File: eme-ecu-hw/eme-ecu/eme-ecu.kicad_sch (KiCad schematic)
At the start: 11 parts, among them U1 ACS712xLCTR-30A

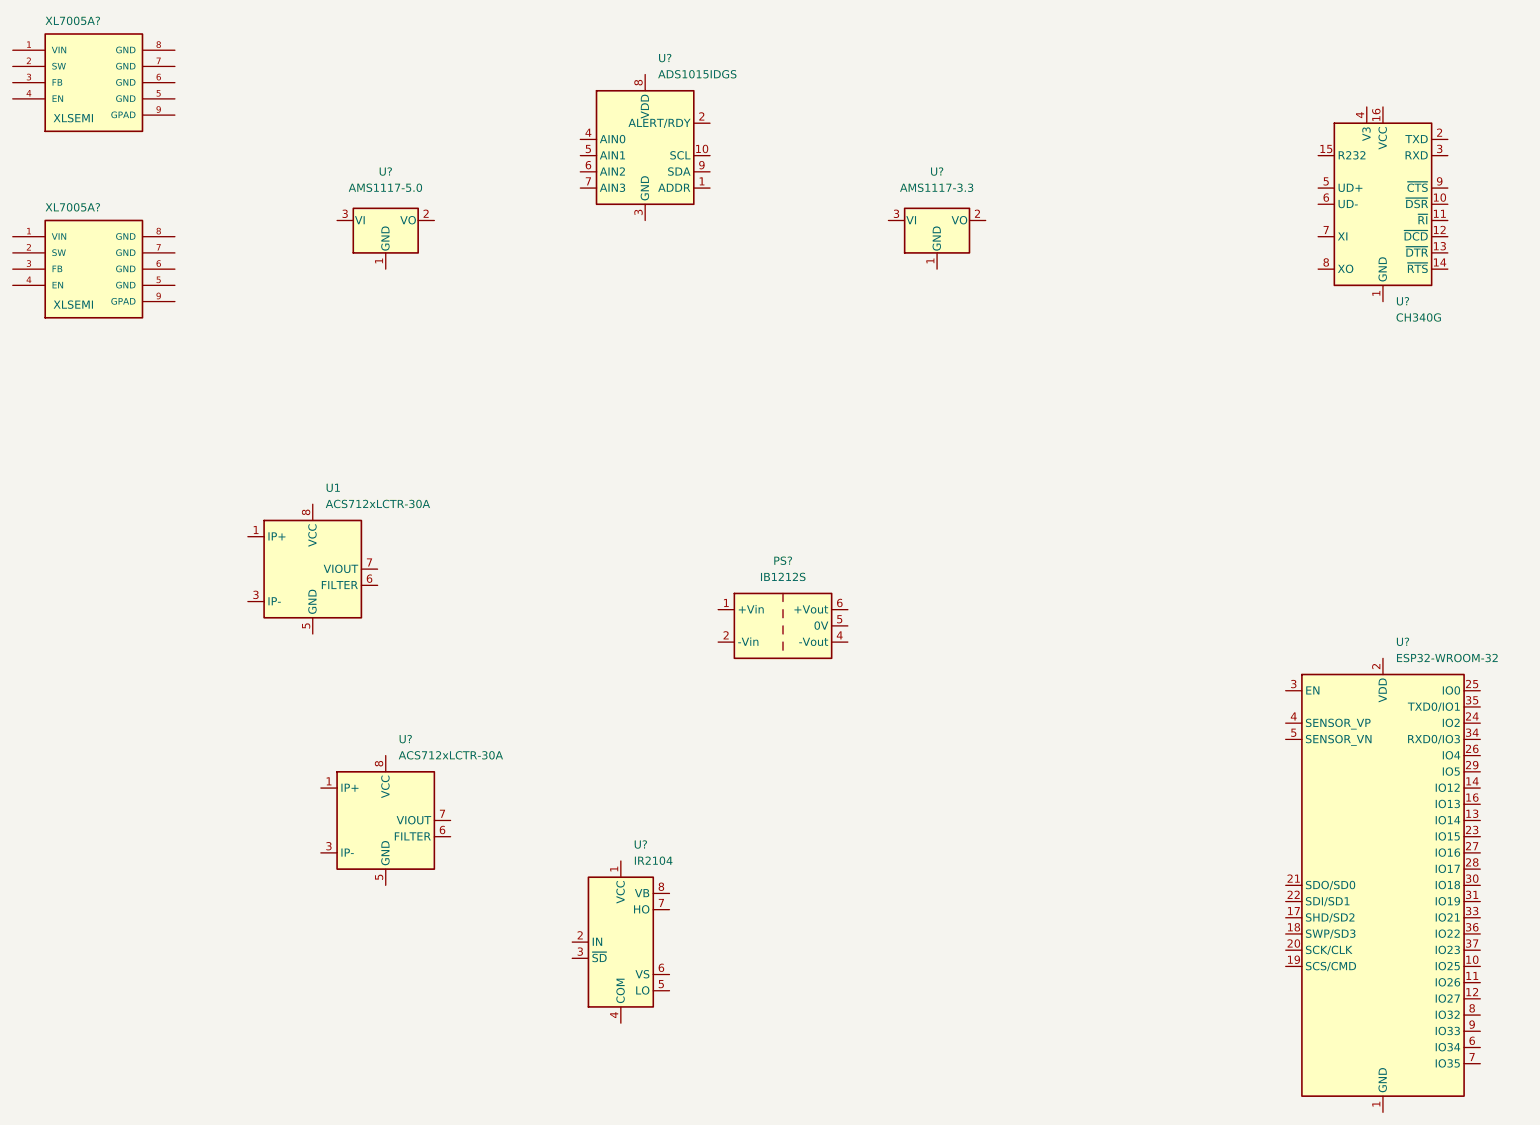
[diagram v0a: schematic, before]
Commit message: Added part list diodes
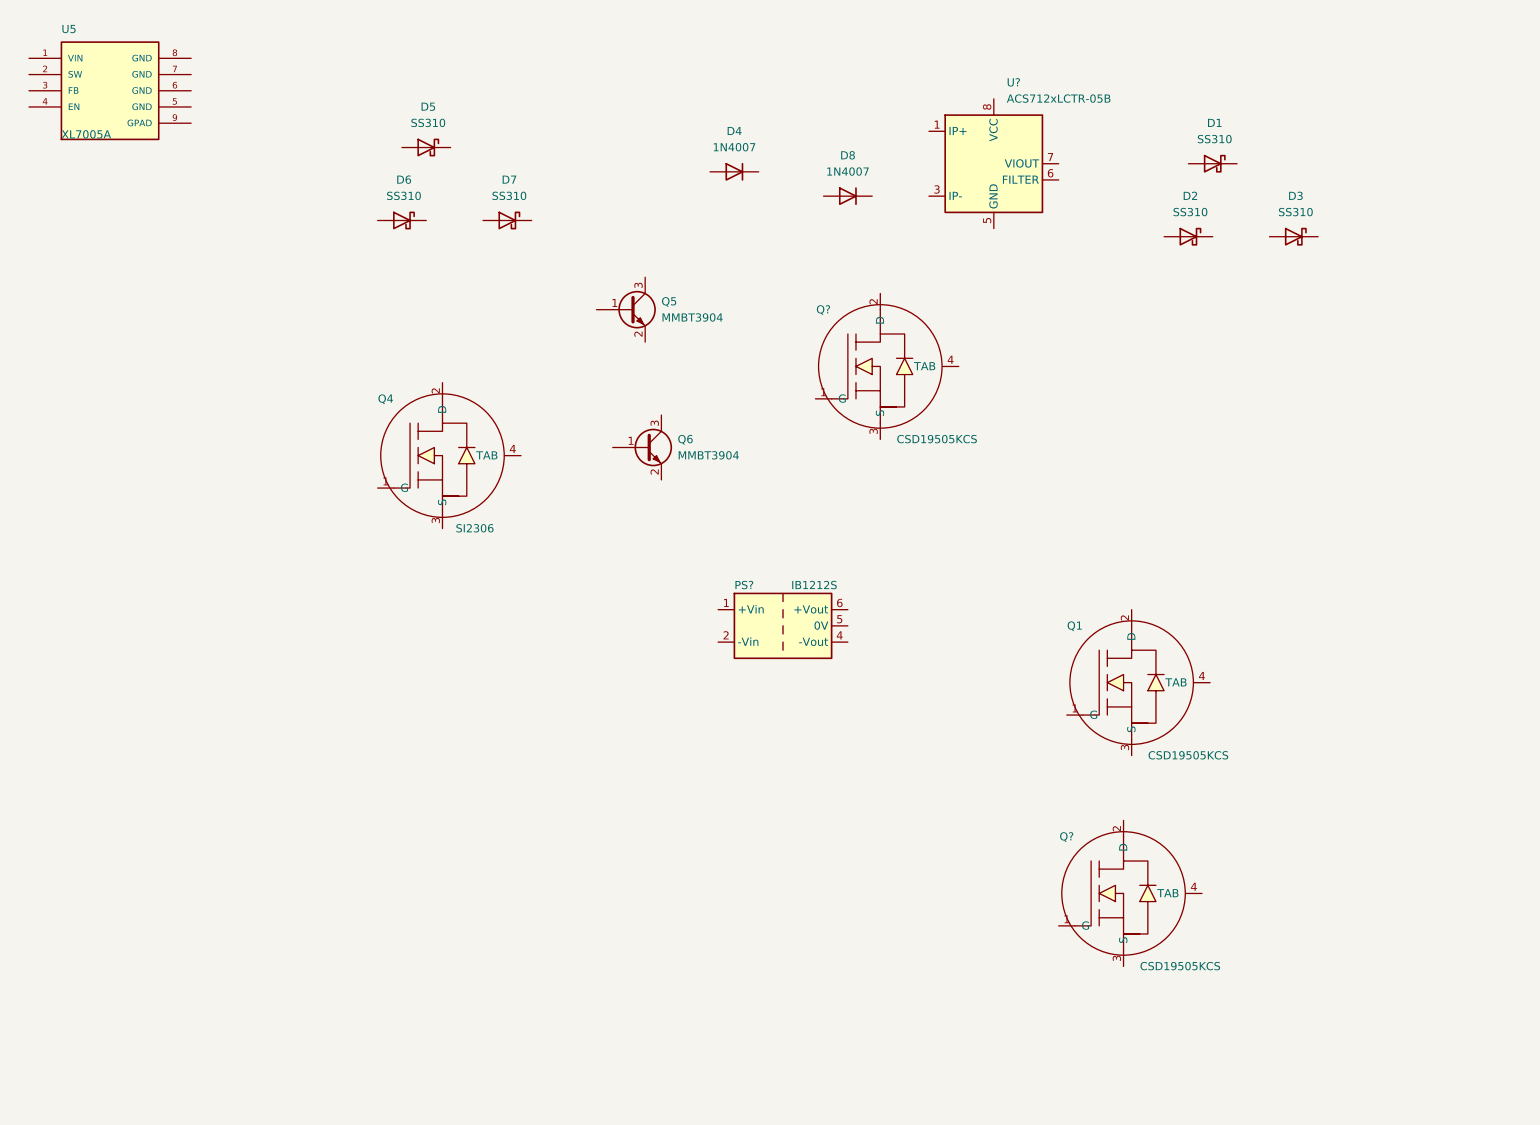
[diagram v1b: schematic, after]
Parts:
- removed U1, U?: ACS712xLCTR-30A, Package_SO:SOIC-8_3.9x4.9mm_P1.27mm, symbol Sensor_Current:ACS712xLCTR-30A
- removed U?: ADS1015IDGS, Package_SO:TSSOP-10_3x3mm_P0.5mm, symbol Analog_ADC:ADS1015IDGS
- removed U?: IR2104, symbol Driver_FET:IR2104
- removed U?: AMS1117-3.3, Package_TO_SOT_SMD:SOT-223-3_TabPin2, symbol Regulator_Linear:AMS1117-3.3
- removed U?: CH340G, Package_SO:SOIC-16_3.9x9.9mm_P1.27mm, symbol Interface_USB:CH340G
- removed U?: ESP32-WROOM-32, RF_Module:ESP32-WROOM-32, symbol RF_Module:ESP32-WROOM-32
- removed U?: AMS1117-5.0, Package_TO_SOT_SMD:SOT-223-3_TabPin2, symbol Regulator_Linear:AMS1117-5.0
- removed XL7005A? (x2): XL7005A, Package_SO:TSSOP-8_3x3mm_P0.65mm, symbol Custom BUCK DC DC:XL7005A
- added D1, D2, D3, D5, D6, D7: SS310, Diode_SMD:D_SMA, symbol Diode:CDBA3100-HF
- added D4, D8: 1N4007, Diode_THT:D_DO-41_SOD81_P10.16mm_Horizontal, symbol Diode:1N4007
- added Q1, Q? (x2): CSD19505KCS, Package_TO_SOT_THT:TO-220-3_Vertical, symbol Custom BUCK DC DC:CSD19505KCS
- added Q4: SI2306, Package_TO_SOT_SMD:SOT-23, symbol Custom BUCK DC DC:CSD19505KCS
- added Q5, Q6: MMBT3904, Package_TO_SOT_SMD:SOT-23, symbol Transistor_BJT:MMBT3904
- added U5: XL7005A, Package_SO:TSSOP-8_3x3mm_P0.65mm, symbol Custom BUCK DC DC:XL7005A
- added U?: ACS712xLCTR-05B, Package_SO:SOIC-8_3.9x4.9mm_P1.27mm, symbol Sensor_Current:ACS712xLCTR-05B
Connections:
- new net: U?.1 (IP+), U?.2 (IP+)
- new net: U?.3 (IP-), U?.4 (IP-)
